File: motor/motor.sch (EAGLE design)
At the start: 3 parts

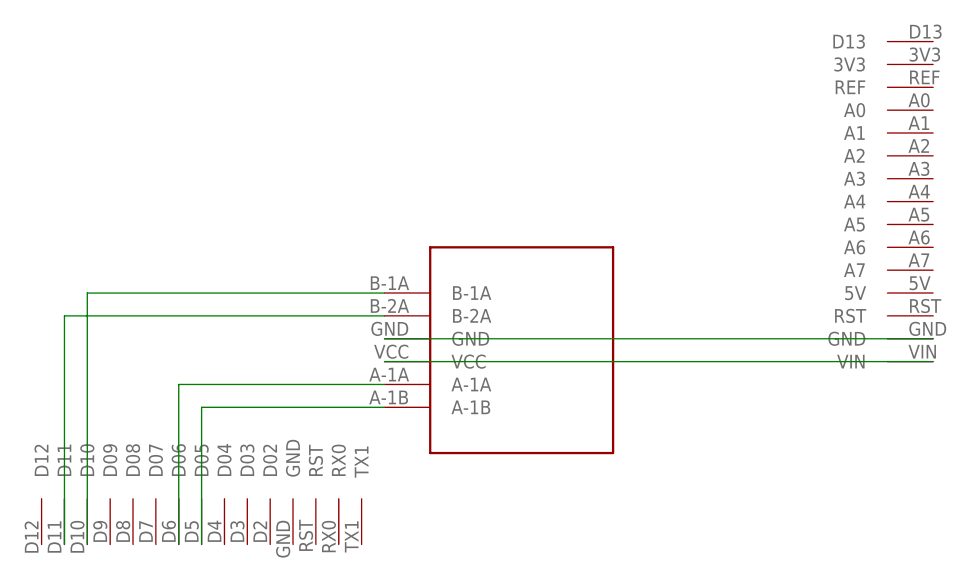
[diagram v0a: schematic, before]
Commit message: Updated Boards for New Configuration
Bluetooth board has been rearranged to accommodate board slot-in
Motor Control Board flipped to be in the right spot
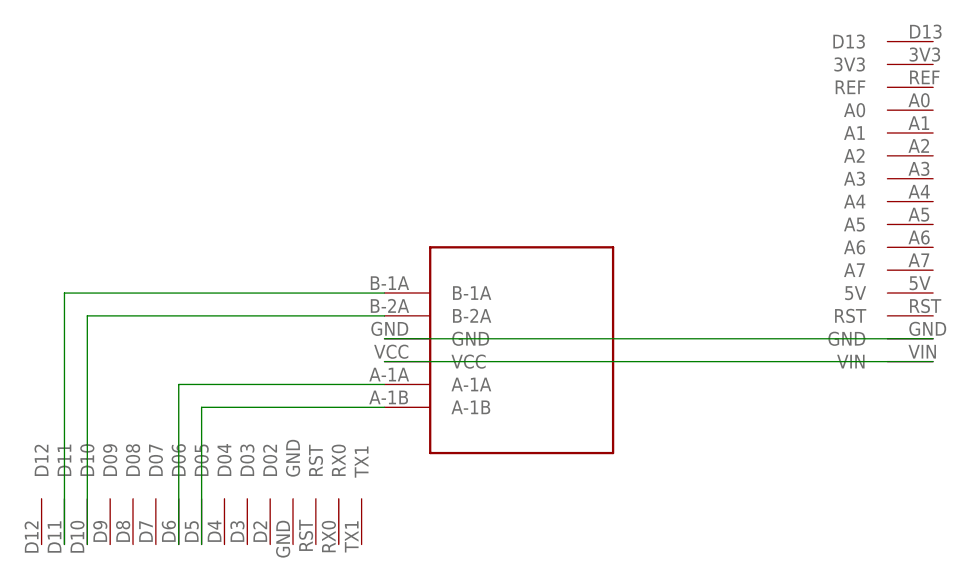
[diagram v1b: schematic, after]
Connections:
- net N$3: now also U$2.B-1A; no longer U$2.B-2A
- net N$4: now also U$2.B-2A; no longer U$2.B-1A
